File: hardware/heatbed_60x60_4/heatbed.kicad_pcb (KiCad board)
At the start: 2 copper layers, 60 x 60 mm, 1 part, among them J1 PWR

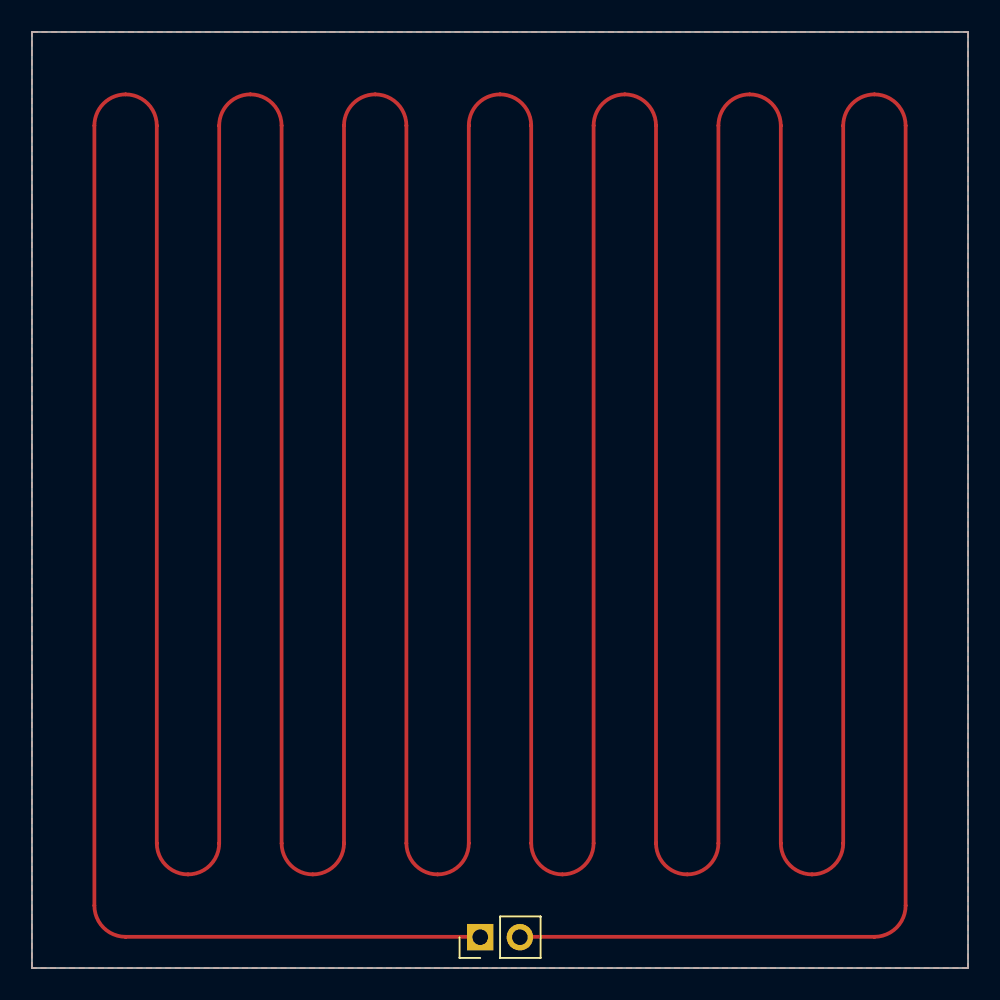
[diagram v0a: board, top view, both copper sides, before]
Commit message: Further increase tracks' widths
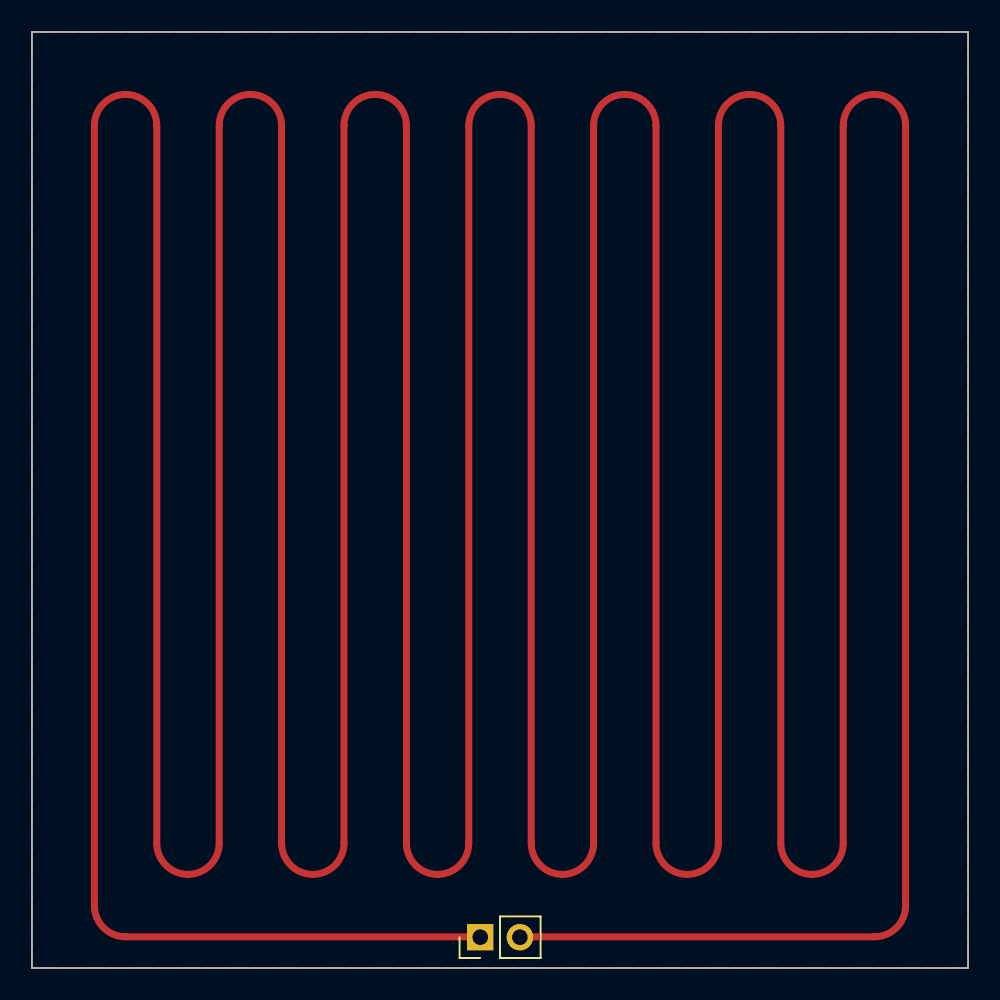
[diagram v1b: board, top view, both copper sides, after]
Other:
- board text added: "Width: 0.449 mm | Length: 785.52 mm | Resistance: 1.51 Ω"
- board text removed: "Width: 0.241 mm | Length: 785.52 mm | Resistance: 2.67 Ω"

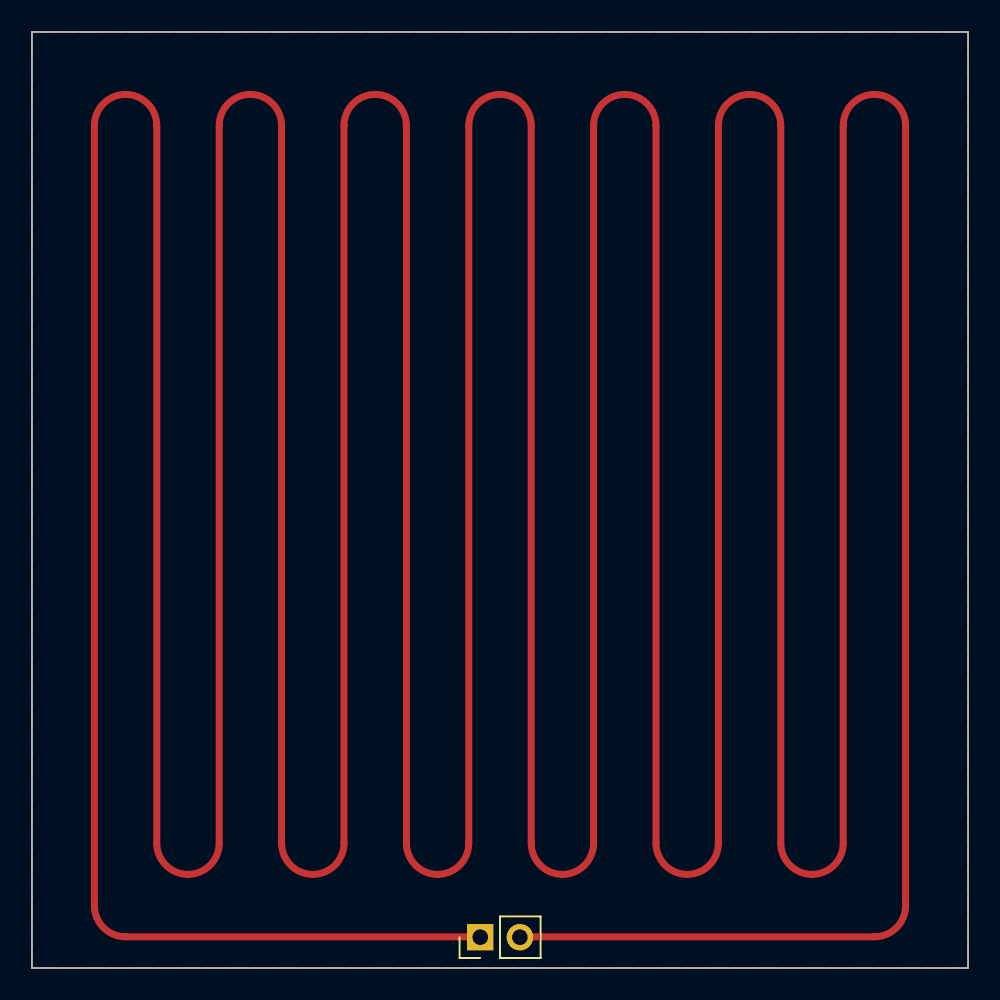
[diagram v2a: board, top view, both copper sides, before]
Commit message: Increase holes' diameters
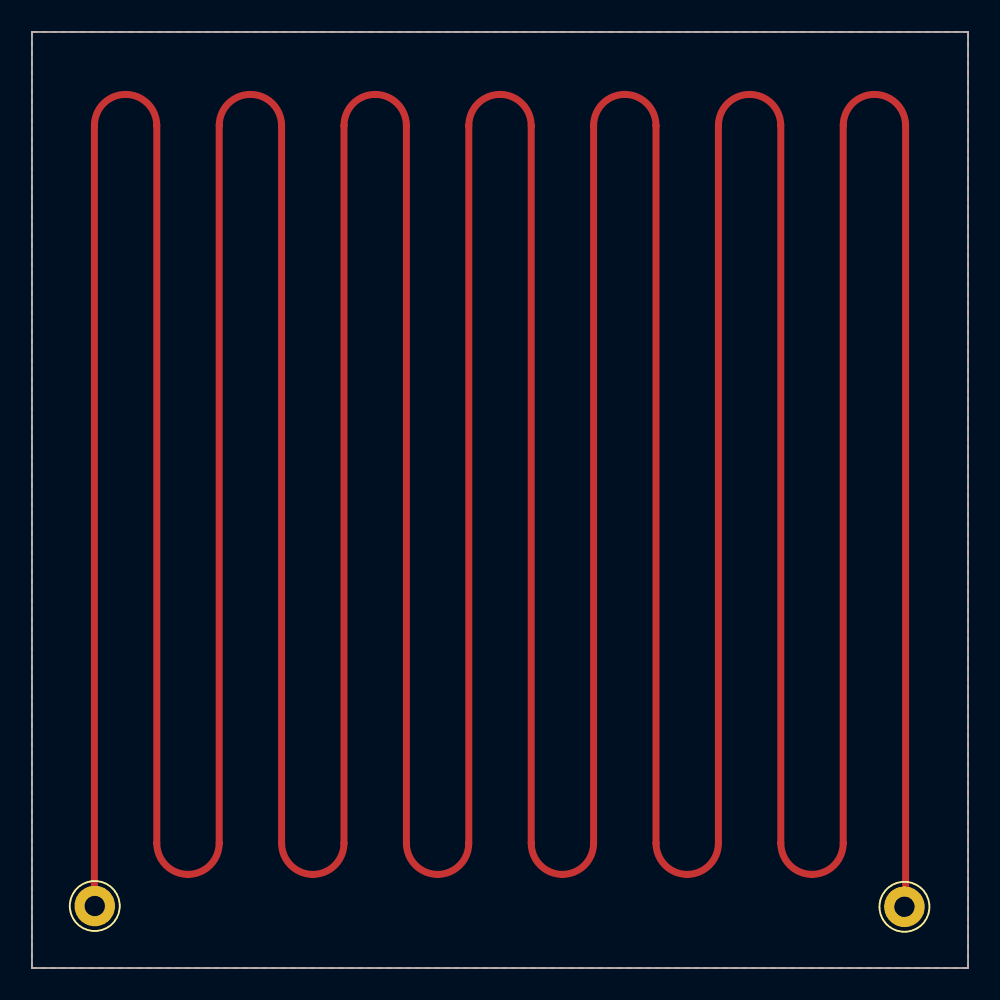
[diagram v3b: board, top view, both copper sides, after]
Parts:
- added J2: Conn_01x01, Connector_Pin:Pin_D1.3mm_L11.0mm, F.Cu at (174.9, 129.1)
- J1: value PWR -> Conn_01x01; footprint Connector_PinHeader_2.54mm:PinHeader_1x02_P2.54mm_Vertical -> Connector_Pin:Pin_D1.3mm_L11.0mm
- moved J1 24.8 mm to (123.0, 129.0), turned to 0 degrees
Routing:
- net Net-(J1-Pin_1): track 783.2 -> 731.7 mm
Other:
- board text removed: "Width: 0.449 mm | Length: 785.52 mm | Resistance: 1.51 Ω"
